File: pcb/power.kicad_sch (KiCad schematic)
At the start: 37 parts

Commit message: start adding processor fpga
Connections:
- net VCC: now also R?.1, U?.24 (PVIN2), U?.6 (PVIN1)
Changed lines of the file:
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@@
   (junction (at 69.85 60.96) (diameter 0.9144) (color 0 0 0 0))
   (junction (at 80.01 88.9) (diameter 0.9144) (color 0 0 0 0))
+  (junction (at 86.36 59.69) (diameter 0.9144) (color 0 0 0 0))
+  (junction (at 91.44 59.69) (diameter 0.9144) (color 0 0 0 0))
   (junction (at 91.44 88.9) (diameter 0.9144) (color 0 0 0 0))
   (junction (at 104.14 66.04) (diameter 0.9144) (color 0 0 0 0))
@@
     (stroke (width 0) (type solid) (color 0 0 0 0))
   )
-  (wire (pts (xy 86.36 46.99) (xy 86.36 60.96))
-    (stroke (width 0) (type solid) (color 0 0 0 0))
-  )
-  (wire (pts (xy 90.17 59.69) (xy 110.49 59.69))
-    (stroke (width 0) (type solid) (color 0 0 0 0))
-  )
-  (wire (pts (xy 91.44 60.96) (xy 91.44 80.01))
+  (wire (pts (xy 86.36 46.99) (xy 86.36 59.69))
+    (stroke (width 0) (type solid) (color 0 0 0 0))
+  )
+  (wire (pts (xy 86.36 59.69) (xy 86.36 60.96))
+    (stroke (width 0) (type solid) (color 0 0 0 0))
+  )
+  (wire (pts (xy 86.36 59.69) (xy 91.44 59.69))
+    (stroke (width 0) (type solid) (color 0 0 0 0))
+  )
+  (wire (pts (xy 91.44 59.69) (xy 91.44 80.01))
+    (stroke (width 0) (type solid) (color 0 0 0 0))
+  )
+  (wire (pts (xy 91.44 59.69) (xy 110.49 59.69))
     (stroke (width 0) (type solid) (color 0 0 0 0))
   )
@@
     (pin "1")
   )
-  (symbol (lib_id "power:+3.3V") (at 80.01 44.45 0) (unit 1)
-    (in_bom yes) (on_board yes)
+  (symbol (lib_id "power:+3V3") (at 80.01 44.45 0) (unit 1)
+    (in_bom yes) (on_board yes) (fields_autoplaced)
     (property "Reference" "#PWR?" (id 0) (at 80.01 48.26 0)
       (effects (font (size 1.27 1.27)) hide)
     )
-    (property "Value" "+3.3V" (id 1) (at 80.01 40.64 0))
+    (property "Value" "+3V3" (id 1) (at 80.01 40.64 0))
     (property "Footprint" "" (id 2) (at 80.01 44.45 0)
       (effects (font (size 1.27 1.27)) hide)
@@
   )
   (symbol (lib_id "power:+1V2") (at 233.68 44.45 0) (unit 1)
-    (in_bom yes) (on_board yes)
+    (in_bom yes) (on_board yes) (fields_autoplaced)
     (property "Reference" "#PWR?" (id 0) (at 233.68 48.26 0)
       (effects (font (size 1.27 1.27)) hide)
@@
     (pin "1")
   )
-  (symbol (lib_id "power:+3.3V") (at 248.92 44.45 0) (unit 1)
-    (in_bom yes) (on_board yes)
+  (symbol (lib_id "power:+3V3") (at 248.92 44.45 0) (unit 1)
+    (in_bom yes) (on_board yes) (fields_autoplaced)
     (property "Reference" "#PWR?" (id 0) (at 248.92 48.26 0)
       (effects (font (size 1.27 1.27)) hide)
     )
-    (property "Value" "+3.3V" (id 1) (at 248.92 40.64 0))
+    (property "Value" "+3V3" (id 1) (at 248.92 40.64 0))
     (property "Footprint" "" (id 2) (at 248.92 44.45 0)
       (effects (font (size 1.27 1.27)) hide)

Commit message: start associating footprints
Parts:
- C51: renamed from C?; footprint (none) -> Capacitor_SMD:CP_Elec_6.3x7.7; Ref (none) -> GYA1E101MCW1GS
- C52: renamed from C?; footprint (none) -> Capacitor_SMD:C_1210_3225Metric; Ref (none) -> EMK325BJ476MM-P
- C53: renamed from C?; footprint (none) -> Capacitor_SMD:C_0805_2012Metric; Ref (none) -> GRM219R61C226ME1K
- C54: renamed from C?; value 100nF -> 0.1uF; footprint (none) -> Capacitor_SMD:C_0603_1608Metric; Ref (none) -> 0603YC104J4T4A
- C55, C63, C64, C68: renamed from C?; footprint (none) -> Capacitor_SMD:C_0603_1608Metric
- C56: renamed from C?; footprint (none) -> Capacitor_SMD:C_0603_1608Metric; Ref (none) -> 0603YC104J4T4A
- C57: renamed from C?; footprint (none) -> Capacitor_SMD:C_1210_3225Metric; Ref (none) -> 12106D107MAT2A
- C58, C59, C60, C69, C70: renamed from C?; footprint (none) -> Capacitor_SMD:C_1210_3225Metric
- C61: renamed from C?; footprint (none) -> Capacitor_SMD:C_0805_2012Metric
- C62: renamed from C?; value 100nF -> 0.1uF; footprint (none) -> Capacitor_SMD:C_0603_1608Metric
- C65: renamed from C?; value 2.2uF -> 4.7uF; footprint (none) -> Capacitor_SMD:C_0402_1005Metric
- C66, C67: renamed from C?; footprint (none) -> Capacitor_SMD:C_0402_1005Metric
- L1: renamed from L?; footprint (none) -> Inductor_SMD:IND_XAL6030-561MEB; Ref (none) -> XAL6030-561MEC
- L2: renamed from L?; footprint (none) -> Inductor_SMD:IND_XAL6030-122MEB; Ref (none) -> XAL6030-122MEC
- gave numbers to parts that had none: 15

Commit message: add tps541620 footprint
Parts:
- R19, R20, R21, R22, R23, R24, R25, R26, R27, R28, R29, R30, R31: footprint (none) -> Resistor_SMD:R_0402_1005Metric
- U10: footprint (none) -> Converter_DCDC:TPS541620
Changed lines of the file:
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@@
       (effects (font (size 1.27 1.27)) (justify left))
     )
-    (property "Footprint" "" (id 2) (at 80.01 82.55 0)
+    (property "Footprint" "Resistor_SMD:R_0402_1005Metric" (id 2) (at 80.01 82.55 0)
       (effects (font (size 1.27 1.27)) hide)
     )
@@
       (effects (font (size 1.27 1.27)) (justify left))
     )
-    (property "Footprint" "" (id 2) (at 80.01 95.25 0)
+    (property "Footprint" "Resistor_SMD:R_0402_1005Metric" (id 2) (at 80.01 95.25 0)
       (effects (font (size 1.27 1.27)) hide)
     )
@@
       (effects (font (size 1.27 1.27)) (justify left))
     )
-    (property "Footprint" "" (id 2) (at 91.44 82.55 0)
+    (property "Footprint" "Resistor_SMD:R_0402_1005Metric" (id 2) (at 91.44 82.55 0)
       (effects (font (size 1.27 1.27)) hide)
     )
@@
       (effects (font (size 1.27 1.27)) (justify left))
     )
-    (property "Footprint" "" (id 2) (at 91.44 95.25 0)
+    (property "Footprint" "Resistor_SMD:R_0402_1005Metric" (id 2) (at 91.44 95.25 0)
       (effects (font (size 1.27 1.27)) hide)
     )
@@
       (effects (font (size 1.27 1.27)) (justify left))
     )
-    (property "Footprint" "" (id 2) (at 111.76 99.06 0)
+    (property "Footprint" "Resistor_SMD:R_0402_1005Metric" (id 2) (at 111.76 99.06 0)
       (effects (font (size 1.27 1.27)) hide)
     )
@@
     (property "Reference" "R26" (id 0) (at 114.3 91.44 90))
     (property "Value" "10k" (id 1) (at 118.11 91.44 90))
-    (property "Footprint" "" (id 2) (at 116.84 93.98 0)
+    (property "Footprint" "Resistor_SMD:R_0402_1005Metric" (id 2) (at 116.84 93.98 0)
       (effects (font (size 1.27 1.27)) hide)
     )
@@
       (effects (font (size 1.27 1.27)) (justify left))
     )
-    (property "Footprint" "" (id 2) (at 121.92 99.06 0)
+    (property "Footprint" "Resistor_SMD:R_0402_1005Metric" (id 2) (at 121.92 99.06 0)
       (effects (font (size 1.27 1.27)) hide)
     )
@@
     (property "Reference" "R19" (id 0) (at 177.8 64.77 90))
     (property "Value" "100k" (id 1) (at 177.8 69.85 90))
-    (property "Footprint" "" (id 2) (at 177.8 67.31 0)
+    (property "Footprint" "Resistor_SMD:R_0402_1005Metric" (id 2) (at 177.8 67.31 0)
       (effects (font (size 1.27 1.27)) hide)
     )
@@
     (property "Reference" "R24" (id 0) (at 177.8 82.55 90))
     (property "Value" "100k" (id 1) (at 177.8 87.63 90))
-    (property "Footprint" "" (id 2) (at 177.8 85.09 0)
+    (property "Footprint" "Resistor_SMD:R_0402_1005Metric" (id 2) (at 177.8 85.09 0)
       (effects (font (size 1.27 1.27)) hide)
     )
@@
     (property "Reference" "R20" (id 0) (at 231.14 67.31 0))
     (property "Value" "14k" (id 1) (at 229.87 69.85 0))
-    (property "Footprint" "" (id 2) (at 233.68 67.31 0)
+    (property "Footprint" "Resistor_SMD:R_0402_1005Metric" (id 2) (at 233.68 67.31 0)
       (effects (font (size 1.27 1.27)) hide)
     )
@@
     (property "Reference" "R21" (id 0) (at 231.14 74.93 0))
     (property "Value" "10k" (id 1) (at 229.87 77.47 0))
-    (property "Footprint" "" (id 2) (at 233.68 76.2 0)
+    (property "Footprint" "Resistor_SMD:R_0402_1005Metric" (id 2) (at 233.68 76.2 0)
       (effects (font (size 1.27 1.27)) hide)
     )
@@
     (property "Reference" "R25" (id 0) (at 246.38 85.09 0))
     (property "Value" "56k" (id 1) (at 245.11 87.63 0))
-    (property "Footprint" "" (id 2) (at 248.92 85.09 0)
+    (property "Footprint" "Resistor_SMD:R_0402_1005Metric" (id 2) (at 248.92 85.09 0)
       (effects (font (size 1.27 1.27)) hide)
     )
@@
     (property "Reference" "R27" (id 0) (at 246.38 92.71 0))
     (property "Value" "10k" (id 1) (at 245.11 95.25 0))
-    (property "Footprint" "" (id 2) (at 248.92 93.98 0)
+    (property "Footprint" "Resistor_SMD:R_0402_1005Metric" (id 2) (at 248.92 93.98 0)
       (effects (font (size 1.27 1.27)) hide)
     )
@@
     (property "Reference" "U10" (id 0) (at 146.05 52.07 0))
     (property "Value" "TPS541620" (id 1) (at 146.05 54.61 0))
-    (property "Footprint" "" (id 2) (at 146.05 50.8 0)
-      (effects (font (size 1.27 1.27)) hide)
-    )
+    (property "Footprint" "Converter_DCDC:TPS541620" (id 2) (at 146.05 50.8 0)
+      (effects (font (size 1.27 1.27)) hide)
+    )

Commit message: add components to pcb
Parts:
- L1: footprint Inductor_SMD:IND_XAL6030-561MEB -> XAL6030-561MEB:IND_XAL6030-561MEB
- L2: footprint Inductor_SMD:IND_XAL6030-122MEB -> XAL6030-122MEB:IND_XAL6030-122MEB
- NT1: footprint (none) -> NetTie:NetTie-2_SMD_Pad0.5mm
- U10: footprint Converter_DCDC:TPS541620 -> TPS541620:TPS541620; now in the parts list
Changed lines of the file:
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@@
-(kicad_sch (version 20210126) (generator eeschema)
+(kicad_sch (version 20210406) (generator eeschema)
   (paper "A4")
   (junction (at 26.67 46.99) (diameter 0.9144) (color 0 0 0 0))
@@
     (property "Reference" "NT1" (id 0) (at 52.07 102.87 0))
     (property "Value" "NetTie_2" (id 1) (at 52.07 105.41 0))
-    (property "Footprint" "" (id 2) (at 52.07 106.68 0)
+    (property "Footprint" "NetTie:NetTie-2_SMD_Pad0.5mm" (id 2) (at 52.07 106.68 0)
       (effects (font (size 1.27 1.27)) hide)
     )
@@
     (property "Reference" "L1" (id 0) (at 194.31 49.53 90))
     (property "Value" "560nH" (id 1) (at 194.31 52.07 90))
-    (property "Footprint" "Inductor_SMD:IND_XAL6030-561MEB" (id 2) (at 194.31 54.61 0)
+    (property "Footprint" "XAL6030-561MEB:IND_XAL6030-561MEB" (id 2) (at 194.31 54.61 0)
       (effects (font (size 1.27 1.27)) hide)
     )
@@
     (property "Reference" "L2" (id 0) (at 194.31 76.2 90))
     (property "Value" "1.2uH" (id 1) (at 194.31 78.74 90))
-    (property "Footprint" "Inductor_SMD:IND_XAL6030-122MEB" (id 2) (at 194.31 81.28 0)
+    (property "Footprint" "XAL6030-122MEB:IND_XAL6030-122MEB" (id 2) (at 194.31 81.28 0)
       (effects (font (size 1.27 1.27)) hide)
     )
@@
   )
   (symbol (lib_id "Regulator_Switching:TPS541620") (at 146.05 50.8 0) (unit 1)
-    (in_bom no) (on_board no) (fields_autoplaced)
+    (in_bom yes) (on_board yes) (fields_autoplaced)
     (property "Reference" "U10" (id 0) (at 146.05 52.07 0))
     (property "Value" "TPS541620" (id 1) (at 146.05 54.61 0))
-    (property "Footprint" "Converter_DCDC:TPS541620" (id 2) (at 146.05 50.8 0)
-      (effects (font (size 1.27 1.27)) hide)
-    )
+    (property "Footprint" "TPS541620:TPS541620" (id 2) (at 146.05 50.8 0)
+      (effects (font (size 1.27 1.27)) hide)
+    )

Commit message: keep working on the pcb
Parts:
- added C47: 100uF, Capacitor_SMD:C_1210_3225Metric, symbol Device:C_Small
- C55: footprint Capacitor_SMD:C_0603_1608Metric -> Capacitor_SMD:C_0402_1005Metric; Ref (none) -> 04025C104KAT4A
- C56: footprint Capacitor_SMD:C_0603_1608Metric -> Capacitor_SMD:C_0402_1005Metric; Ref 0603YC104J4T4A -> 04025C104KAT4A
- C63, C64, C68: footprint Capacitor_SMD:C_0603_1608Metric -> Capacitor_SMD:C_0402_1005Metric
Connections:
- net +3V3: now also C47.1
- net GND: now also C47.2
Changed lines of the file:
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@@
   (junction (at 212.09 64.77) (diameter 0.9144) (color 0 0 0 0))
   (junction (at 214.63 81.28) (diameter 0.9144) (color 0 0 0 0))
+  (junction (at 214.63 91.44) (diameter 0.9144) (color 0 0 0 0))
   (junction (at 223.52 54.61) (diameter 0.9144) (color 0 0 0 0))
   (junction (at 223.52 64.77) (diameter 0.9144) (color 0 0 0 0))
+  (junction (at 226.06 81.28) (diameter 0.9144) (color 0 0 0 0))
   (junction (at 233.68 54.61) (diameter 0.9144) (color 0 0 0 0))
   (junction (at 233.68 63.5) (diameter 0.9144) (color 0 0 0 0))
@@
     (stroke (width 0) (type solid) (color 0 0 0 0))
   )
-  (wire (pts (xy 214.63 81.28) (xy 248.92 81.28))
+  (wire (pts (xy 214.63 81.28) (xy 226.06 81.28))
     (stroke (width 0) (type solid) (color 0 0 0 0))
   )
@@
   )
   (wire (pts (xy 223.52 64.77) (xy 223.52 110.49))
+    (stroke (width 0) (type solid) (color 0 0 0 0))
+  )
+  (wire (pts (xy 226.06 81.28) (xy 226.06 83.82))
+    (stroke (width 0) (type solid) (color 0 0 0 0))
+  )
+  (wire (pts (xy 226.06 81.28) (xy 248.92 81.28))
+    (stroke (width 0) (type solid) (color 0 0 0 0))
+  )
+  (wire (pts (xy 226.06 88.9) (xy 226.06 91.44))
+    (stroke (width 0) (type solid) (color 0 0 0 0))
+  )
+  (wire (pts (xy 226.06 91.44) (xy 214.63 91.44))
     (stroke (width 0) (type solid) (color 0 0 0 0))
   )
@@
   )
   (symbol (lib_id "Device:C_Small") (at 69.85 52.07 0) (unit 1)
-    (in_bom yes) (on_board yes) (fields_autoplaced)
+    (in_bom yes) (on_board yes)
     (property "Reference" "C55" (id 0) (at 72.39 51.4349 0)
       (effects (font (size 1.27 1.27)) (justify left))
@@
       (effects (font (size 1.27 1.27)) (justify left))
     )
-    (property "Footprint" "Capacitor_SMD:C_0603_1608Metric" (id 2) (at 69.85 52.07 0)
+    (property "Footprint" "Capacitor_SMD:C_0402_1005Metric" (id 2) (at 69.85 52.07 0)
       (effects (font (size 1.27 1.27)) hide)
     )
@@
       (effects (font (size 1.27 1.27)) hide)
     )
+    (property "Ref" "04025C104KAT4A" (id 4) (at 74.93 55.88 0)
+      (effects (font (size 0.5 0.5)))
+    )
     (pin "1")
     (pin "2")
@@
       (effects (font (size 1.27 1.27)) (justify left))
     )
-    (property "Footprint" "Capacitor_SMD:C_0603_1608Metric" (id 2) (at 69.85 66.04 0)
+    (property "Footprint" "Capacitor_SMD:C_0402_1005Metric" (id 2) (at 69.85 66.04 0)
       (effects (font (size 1.27 1.27)) hide)
     )
@@
     (property "Reference" "C56" (id 0) (at 172.72 50.8 90))
     (property "Value" "0.1uF" (id 1) (at 172.72 53.34 90))
-    (property "Footprint" "Capacitor_SMD:C_0603_1608Metric" (id 2) (at 172.72 59.69 0)
+    (property "Footprint" "Capacitor_SMD:C_0402_1005Metric" (id 2) (at 172.72 59.69 0)
       (effects (font (size 1.27 1.27)) hide)
     )
@@
       (effects (font (size 1.27 1.27)) hide)
     )
-    (property "Ref" "0603YC104J4T4A" (id 4) (at 172.72 55.88 90)
+    (property "Ref" "04025C104KAT4A" (id 4) (at 172.72 55.88 90)
       (effects (font (size 0.5 0.5)))
     )
@@
     (pin "2")
   )
+  (symbol (lib_id "Device:C_Small") (at 226.06 86.36 0) (unit 1)
+    (in_bom yes) (on_board yes) (fields_autoplaced)
+    (property "Reference" "C47" (id 0) (at 228.6 85.7249 0)
+      (effects (font (size 1.27 1.27)) (justify left))
+    )
+    (property "Value" "100uF" (id 1) (at 228.6 88.2649 0)
+      (effects (font (size 1.27 1.27)) (justify left))
+    )
+    (property "Footprint" "Capacitor_SMD:C_1210_3225Metric" (id 2) (at 226.06 86.36 0)
+      (effects (font (size 1.27 1.27)) hide)
+    )
+    (property "Datasheet" "~" (id 3) (at 226.06 86.36 0)
+      (effects (font (size 1.27 1.27)) hide)
+    )
+    (pin "1")
+    (pin "2")
+  )
   (symbol (lib_id "Device:C_Small") (at 242.57 67.31 180) (unit 1)
     (in_bom yes) (on_board yes)
@@
       (effects (font (size 1.27 1.27)) (justify right))
     )
-    (property "Footprint" "Capacitor_SMD:C_0603_1608Metric" (id 2) (at 242.57 67.31 0)
+    (property "Footprint" "Capacitor_SMD:C_0402_1005Metric" (id 2) (at 242.57 67.31 0)
       (effects (font (size 1.27 1.27)) hide)
     )
@@
       (effects (font (size 1.27 1.27)) (justify right))
     )
-    (property "Footprint" "Capacitor_SMD:C_0603_1608Metric" (id 2) (at 257.81 85.09 0)
-      (effects (font (size 1.27 1.27)) hide)
-    )
+    (property "Footprint" "Capacitor_SMD:C_0402_1005Metric" (id 2) (at 257.81 85.09 0)
+      (effects (font (size 1.27 1.27)) hide)
+    )

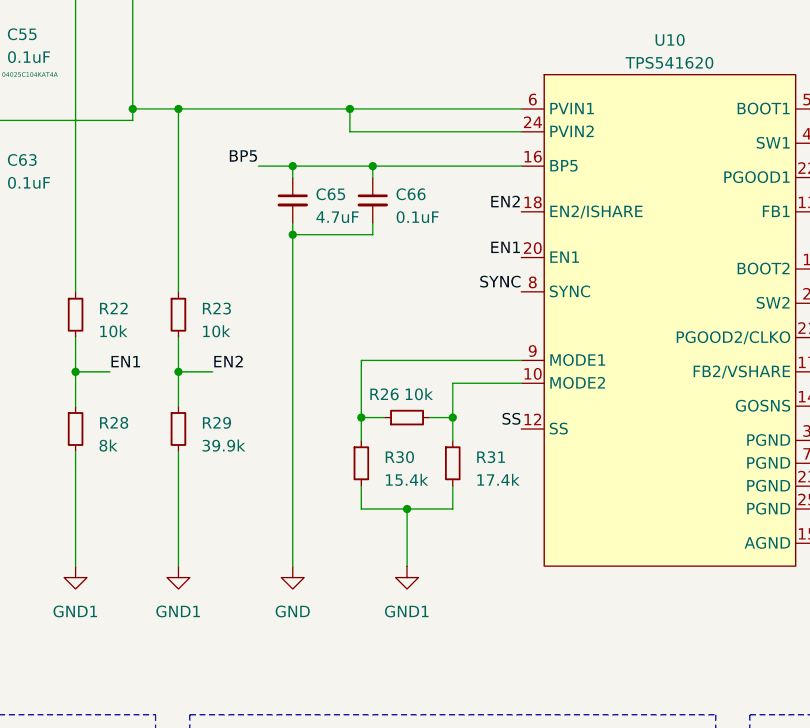
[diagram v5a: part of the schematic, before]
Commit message: add traces for the power supply
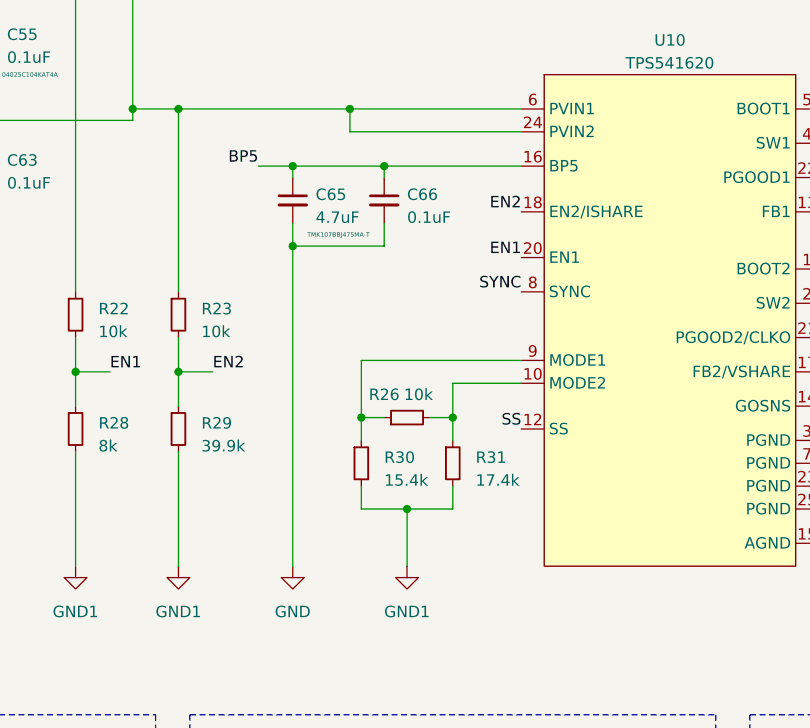
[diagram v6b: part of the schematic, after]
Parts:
- C65: footprint Capacitor_SMD:C_0402_1005Metric -> Capacitor_SMD:C_0603_1608Metric; Ref (none) -> TMK107BBJ475MA-T
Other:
- moved on the sheet: C66
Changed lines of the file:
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@@
   (junction (at 91.44 88.9) (diameter 0.9144) (color 0 0 0 0))
   (junction (at 104.14 66.04) (diameter 0.9144) (color 0 0 0 0))
-  (junction (at 104.14 73.66) (diameter 0.9144) (color 0 0 0 0))
+  (junction (at 104.14 74.93) (diameter 0.9144) (color 0 0 0 0))
   (junction (at 110.49 59.69) (diameter 0.9144) (color 0 0 0 0))
   (junction (at 111.76 93.98) (diameter 0.9144) (color 0 0 0 0))
-  (junction (at 113.03 66.04) (diameter 0.9144) (color 0 0 0 0))
+  (junction (at 114.3 66.04) (diameter 0.9144) (color 0 0 0 0))
   (junction (at 116.84 104.14) (diameter 0.9144) (color 0 0 0 0))
   (junction (at 121.92 93.98) (diameter 0.9144) (color 0 0 0 0))
@@
     (stroke (width 0) (type solid) (color 0 0 0 0))
   )
-  (wire (pts (xy 104.14 66.04) (xy 113.03 66.04))
+  (wire (pts (xy 104.14 66.04) (xy 114.3 66.04))
     (stroke (width 0) (type solid) (color 0 0 0 0))
   )
@@
     (stroke (width 0) (type solid) (color 0 0 0 0))
   )
-  (wire (pts (xy 104.14 72.39) (xy 104.14 73.66))
-    (stroke (width 0) (type solid) (color 0 0 0 0))
-  )
-  (wire (pts (xy 104.14 73.66) (xy 104.14 110.49))
-    (stroke (width 0) (type solid) (color 0 0 0 0))
-  )
-  (wire (pts (xy 104.14 73.66) (xy 113.03 73.66))
+  (wire (pts (xy 104.14 72.39) (xy 104.14 74.93))
+    (stroke (width 0) (type solid) (color 0 0 0 0))
+  )
+  (wire (pts (xy 104.14 74.93) (xy 104.14 110.49))
+    (stroke (width 0) (type solid) (color 0 0 0 0))
+  )
+  (wire (pts (xy 104.14 74.93) (xy 114.3 74.93))
     (stroke (width 0) (type solid) (color 0 0 0 0))
   )
@@
     (stroke (width 0) (type solid) (color 0 0 0 0))
   )
-  (wire (pts (xy 113.03 66.04) (xy 113.03 67.31))
-    (stroke (width 0) (type solid) (color 0 0 0 0))
-  )
-  (wire (pts (xy 113.03 66.04) (xy 129.54 66.04))
-    (stroke (width 0) (type solid) (color 0 0 0 0))
-  )
-  (wire (pts (xy 113.03 73.66) (xy 113.03 72.39))
+  (wire (pts (xy 114.3 66.04) (xy 114.3 67.31))
+    (stroke (width 0) (type solid) (color 0 0 0 0))
+  )
+  (wire (pts (xy 114.3 66.04) (xy 129.54 66.04))
+    (stroke (width 0) (type solid) (color 0 0 0 0))
+  )
+  (wire (pts (xy 114.3 72.39) (xy 114.3 74.93))
     (stroke (width 0) (type solid) (color 0 0 0 0))
   )
@@
   )
   (symbol (lib_id "Device:C_Small") (at 104.14 69.85 0) (unit 1)
-    (in_bom yes) (on_board yes) (fields_autoplaced)
+    (in_bom yes) (on_board yes)
     (property "Reference" "C65" (id 0) (at 106.68 69.2149 0)
       (effects (font (size 1.27 1.27)) (justify left))
@@
       (effects (font (size 1.27 1.27)) (justify left))
     )
-    (property "Footprint" "Capacitor_SMD:C_0402_1005Metric" (id 2) (at 104.14 69.85 0)
+    (property "Footprint" "Capacitor_SMD:C_0603_1608Metric" (id 2) (at 104.14 69.85 0)
       (effects (font (size 1.27 1.27)) hide)
     )
@@
       (effects (font (size 1.27 1.27)) hide)
     )
-    (pin "1")
-    (pin "2")
-  )
-  (symbol (lib_id "Device:C_Small") (at 113.03 69.85 0) (unit 1)
-    (in_bom yes) (on_board yes) (fields_autoplaced)
-    (property "Reference" "C66" (id 0) (at 115.57 69.2149 0)
-      (effects (font (size 1.27 1.27)) (justify left))
-    )
-    (property "Value" "0.1uF" (id 1) (at 115.57 71.7549 0)
-      (effects (font (size 1.27 1.27)) (justify left))
-    )
-    (property "Footprint" "Capacitor_SMD:C_0402_1005Metric" (id 2) (at 113.03 69.85 0)
-      (effects (font (size 1.27 1.27)) hide)
-    )
-    (property "Datasheet" "~" (id 3) (at 113.03 69.85 0)
+    (property "Ref" "TMK107BBJ475MA-T" (id 4) (at 109.22 73.66 0)
+      (effects (font (size 0.5 0.5)))
+    )
+    (pin "1")
+    (pin "2")
+  )
+  (symbol (lib_id "Device:C_Small") (at 114.3 69.85 0) (unit 1)
+    (in_bom yes) (on_board yes) (fields_autoplaced)
+    (property "Reference" "C66" (id 0) (at 116.84 69.2149 0)
+      (effects (font (size 1.27 1.27)) (justify left))
+    )
+    (property "Value" "0.1uF" (id 1) (at 116.84 71.7549 0)
+      (effects (font (size 1.27 1.27)) (justify left))
+    )
+    (property "Footprint" "Capacitor_SMD:C_0402_1005Metric" (id 2) (at 114.3 69.85 0)
+      (effects (font (size 1.27 1.27)) hide)
+    )
+    (property "Datasheet" "~" (id 3) (at 114.3 69.85 0)
       (effects (font (size 1.27 1.27)) hide)
     )
@@
   )
   (symbol (lib_id "Device:C_Small") (at 242.57 67.31 180) (unit 1)
-    (in_bom yes) (on_board yes)
+    (in_bom yes) (on_board no)
     (property "Reference" "C64" (id 0) (at 238.76 66.6749 0)
       (effects (font (size 1.27 1.27)) (justify right))
@@
   )
   (symbol (lib_id "Device:C_Small") (at 257.81 85.09 180) (unit 1)
-    (in_bom yes) (on_board yes)
+    (in_bom yes) (on_board no)
     (property "Reference" "C68" (id 0) (at 254 84.4549 0)
       (effects (font (size 1.27 1.27)) (justify right))
